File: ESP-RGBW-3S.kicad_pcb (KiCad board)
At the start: 2 copper layers, 66.7 x 48.3 mm, 39 parts, among them J1 12V IN, J2 PROG, J3 LED Str., J4 Temp. S., J5 Light. S., J6 PIR, Q1 IRLML0040TRPBF, Q2 IRLML0040TRPBF, Q3 IRLML0040TRPBF, Q4 IRLML0040TRPBF, SW1 Flash, U2 ESP-12E, U4 DCDC_LM2596

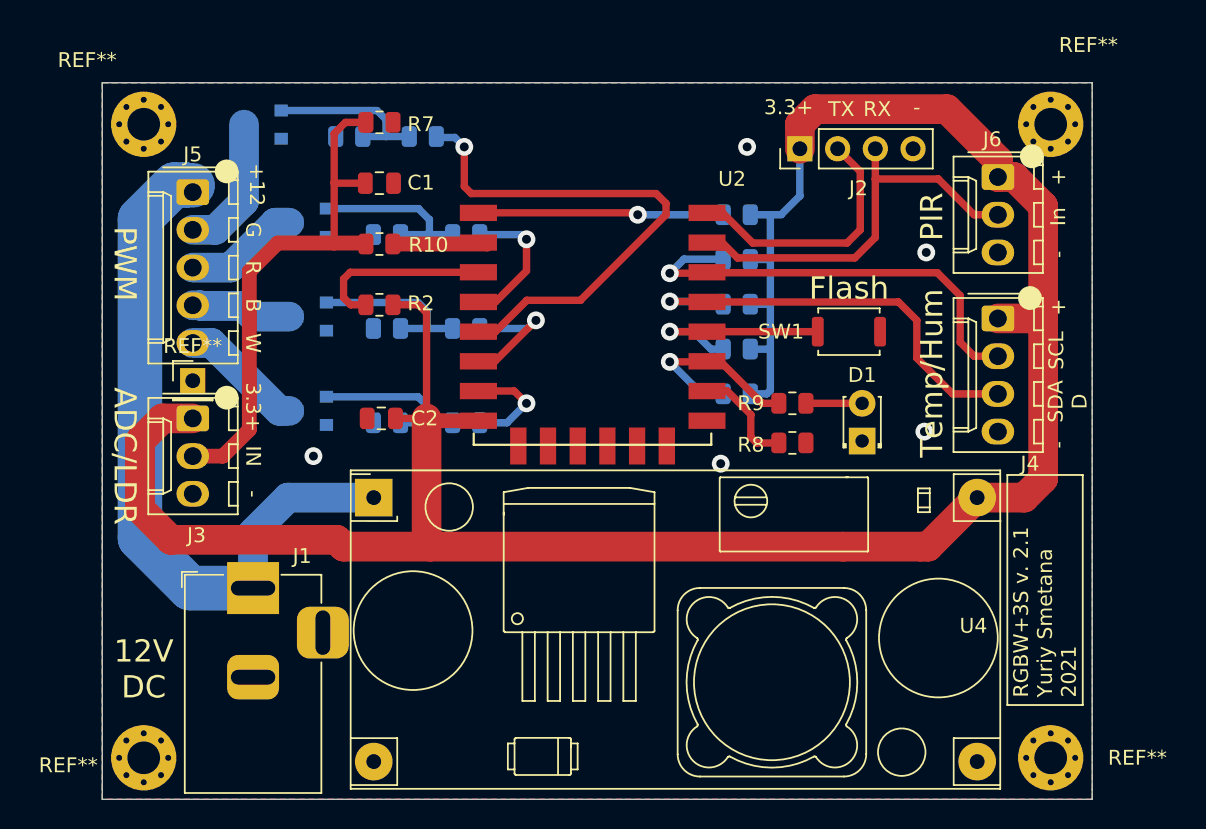
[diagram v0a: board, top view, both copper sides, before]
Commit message: silc correction, optional extra GND for J6
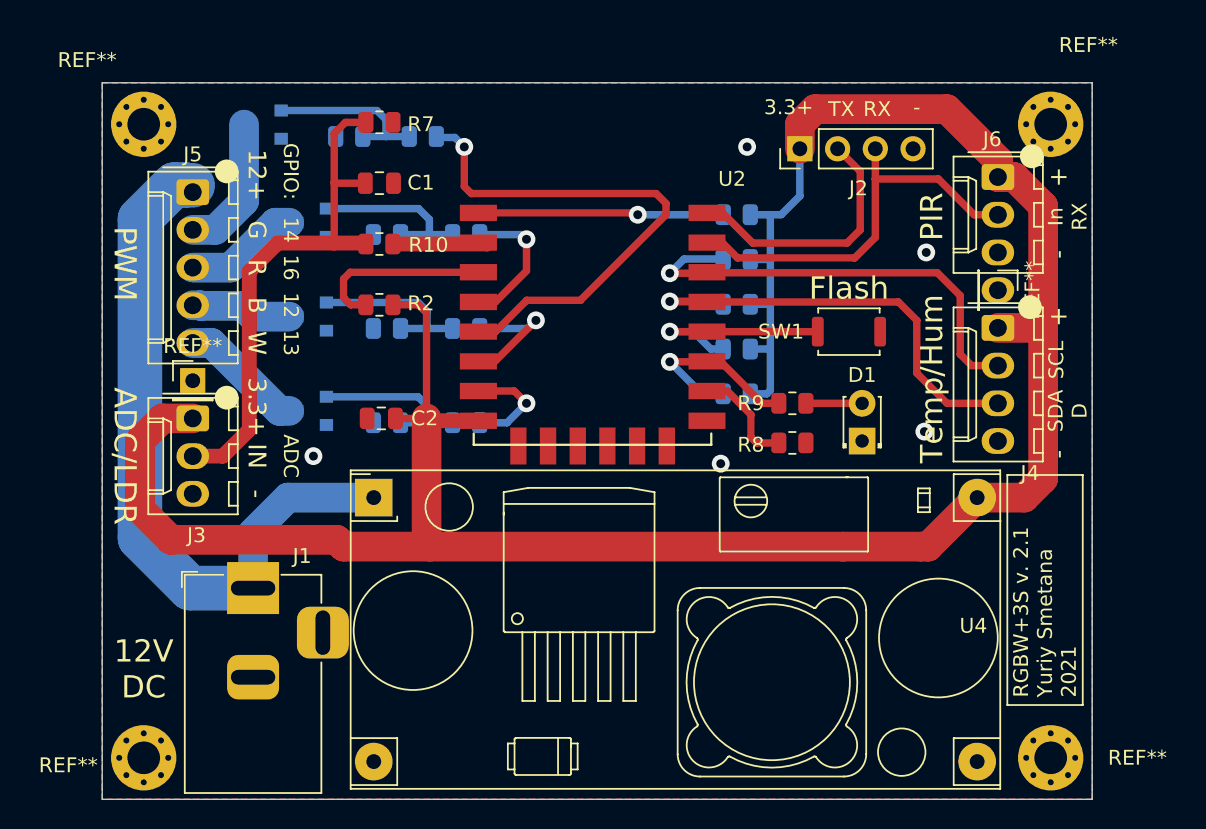
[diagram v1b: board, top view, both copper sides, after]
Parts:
- added REF**: PinHeader_1x01_P2.54mm_Vertical, Connector_PinHeader_2.54mm:PinHeader_1x01_P2.54mm_Vertical, F.Cu at (79.4, 39.4)
- moved J4 0.63 mm to (79.4, 41.9)
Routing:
- net /SDA-DATA: track 30.0 -> 30.8 mm
- net /SCL: track 30.9 -> 31.7 mm
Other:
- board text added: "12"
- board text added: "12+"
- board text added: "13"
- board text added: "14"
- board text added: "16"
- board text added: "ADC"
- board text added: "GPIO:"
- board text added: "In RX"
- board text removed: "+12"
- board text removed: "In"

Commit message: Update ESP-RGBW-3S.kicad_pcb
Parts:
- turned REF** to 270 degrees
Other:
- board text added: "RGBW-3S v. 2.3 Yuriy Smetana 2021"
- board text added: "RX In"
- board text removed: "In RX"
- board text removed: "RGBW+3S v. 2.1 Yuriy Smetana 2021"
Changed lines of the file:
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@@
   (page A4)
   (layers
-    (0 F.Cu signal)
+    (0 F.Cu signal hide)
     (31 B.Cu signal hide)
     (32 B.Adhes user hide)
@@
     (descr "Through hole straight pin header, 1x01, 2.54mm pitch, single row")
     (tags "Through hole pin header THT 1x01 2.54mm single row")
-    (fp_text reference REF** (at 0 -2.33 90) (layer F.SilkS)
+    (fp_text reference REF** (at -0.127 -7.747 90) (layer F.SilkS) hide
       (effects (font (size 1 1) (thickness 0.15)))
     )
@@
       (effects (font (size 1 1) (thickness 0.15)))
     )
-    (pad 6* thru_hole oval (at 0 0 270) (size 1.74 2.2) (drill 1.2) (layers *.Cu *.Mask)
+    (pad 4* thru_hole oval (at 0 0 270) (size 1.74 2.2) (drill 1.2) (layers *.Cu *.Mask)
       (net 1 GND))
     (model ${KISYS3DMOD}/Connector_PinHeader_2.54mm.3dshapes/PinHeader_1x01_P2.54mm_Vertical.wrl
@@
   )
   (module Connector_PinHeader_2.54mm:PinHeader_1x01_P2.54mm_Vertical (layer F.Cu)
-    (at 25.146 45.466)
+    (at 25.146 45.466 270)
     (descr "Through hole straight pin header, 1x01, 2.54mm pitch, single row")
     (tags "Through hole pin header THT 1x01 2.54mm single row")
-    (fp_text reference REF** (at 0 -2.33) (layer F.SilkS)
-      (effects (font (size 1 1) (thickness 0.15)))
-    )
-    (fp_text value PinHeader_1x01_P2.54mm_Vertical (at 0 2.33) (layer F.Fab)
-      (effects (font (size 1 1) (thickness 0.15)))
-    )
-    (fp_text user %R (at 0 0 90) (layer F.Fab)
+    (fp_text reference REF** (at 0 7.747 90) (layer F.SilkS) hide
+      (effects (font (size 1 1) (thickness 0.15)))
+    )
+    (fp_text value PinHeader_1x01_P2.54mm_Vertical (at 0 2.33 90) (layer F.Fab)
+      (effects (font (size 1 1) (thickness 0.15)))
+    )
+    (fp_text user %R (at 0 0) (layer F.Fab)
       (effects (font (size 1 1) (thickness 0.15)))
     )
@@
     (fp_line (start 1.8 1.8) (end 1.8 -1.8) (layer F.CrtYd) (width 0.05))
     (fp_line (start 1.8 -1.8) (end -1.8 -1.8) (layer F.CrtYd) (width 0.05))
-    (pad 6* thru_hole rect (at 0 0) (size 1.7 1.7) (drill 1) (layers *.Cu *.Mask)
+    (pad 6* thru_hole oval (at 0 0 270) (size 1.74 2.2) (drill 1.2) (layers *.Cu *.Mask)
       (net 1 GND))
     (model ${KISYS3DMOD}/Connector_PinHeader_2.54mm.3dshapes/PinHeader_1x01_P2.54mm_Vertical.wrl
@@
     (descr "Molex KK-254 Interconnect System, old/engineering part number: AE-6410-04A example for new part number: 22-27-2041, 4 Pins (http://www.molex.com/pdm_docs/sd/022272021_sd.pdf), generated with kicad-footprint-generator")
     (tags "connector Molex KK-254 side entry")
-    (fp_text reference J4 (at 9.779 -2.159 180) (layer F.SilkS)
+    (fp_text reference J4 (at 10.16 -2.413 180) (layer F.SilkS)
       (effects (font (size 1 1) (thickness 0.15)))
     )
@@
   (gr_line (start 19.05 73.025) (end 19.05 73.66) (layer Edge.Cuts) (width 0.05))
   (gr_line (start 85.725 73.025) (end 85.725 73.66) (layer Edge.Cuts) (width 0.05))
-  (gr_line (start 85.09 51.816) (end 80.01 51.816) (layer F.SilkS) (width 0.12))
-  (gr_line (start 85.09 67.31) (end 85.09 51.816) (layer F.SilkS) (width 0.12))
+  (gr_line (start 85.09 53.848) (end 80.01 53.848) (layer F.SilkS) (width 0.12))
+  (gr_line (start 85.09 67.31) (end 85.09 53.848) (layer F.SilkS) (width 0.12))
   (gr_line (start 80.01 67.31) (end 85.09 67.31) (layer F.SilkS) (width 0.12))
-  (gr_line (start 80.01 51.816) (end 80.01 67.31) (layer F.SilkS) (width 0.12))
+  (gr_line (start 80.01 53.848) (end 80.01 67.31) (layer F.SilkS) (width 0.12))
   (gr_text JLCJLCJLCJLC (at 29.972 70.866) (layer B.SilkS)
     (effects (font (size 1 1) (thickness 0.15)) (justify mirror))
   )
-  (gr_text "RGBW+3S v. 2.1\nYuriy Smetana\n2021" (at 82.55 66.802 90) (layer F.SilkS)
+  (gr_text "RGBW-3S v. 2.3\nYuriy Smetana\n2021" (at 82.55 66.802 90) (layer F.SilkS)
     (effects (font (size 1 1) (thickness 0.15)) (justify left))
   )
@@
     (effects (font (size 1.2 1.2) (thickness 0.2)))
   )
-  (gr_text "In\nRX" (at 84.074 34.417 90) (layer F.SilkS)
+  (gr_text "RX\nIn" (at 84.074 34.417 90) (layer F.SilkS)
     (effects (font (size 1 1) (thickness 0.2)))
   )
@@
   (segment (start 60.84125 37.27196) (end 60.87046 37.30117) (width 0.5) (layer B.Cu) (net 12))
   (segment (start 58.23204 37.27196) (end 60.84125 37.27196) (width 0.5) (layer B.Cu) (net 12))
-  (segment (start 75.296254 38.195022) (end 76.835 39.733768) (width 0.5) (layer F.Cu) (net 12))
-  (segment (start 59.117022 38.195022) (end 75.296254 38.195022) (width 0.5) (layer F.Cu) (net 12))
+  (segment (start 77.597 44.45) (end 79.375 44.45) (width 0.5) (layer F.Cu) (net 12))
+  (segment (start 76.835 40.513) (end 76.835 43.688) (width 0.5) (layer F.Cu) (net 12))
+  (segment (start 74.517022 38.195022) (end 76.835 40.513) (width 0.5) (layer F.Cu) (net 12))
+  (segment (start 59.117022 38.195022) (end 74.517022 38.195022) (width 0.5) (layer F.Cu) (net 12))
+  (segment (start 76.835 43.688) (end 77.597 44.45) (width 0.5) (layer F.Cu) (net 12))
   (segment (start 59.085 38.163) (end 59.117022 38.195022) (width 0.5) (layer F.Cu) (net 12))
-  (segment (start 76.835 39.733768) (end 76.835 43.688) (width 0.5) (layer F.Cu) (net 12))
-  (segment (start 77.597 44.45) (end 79.375 44.45) (width 0.5) (layer F.Cu) (net 12))
-  (segment (start 76.835 43.688) (end 77.597 44.45) (width 0.5) (layer F.Cu) (net 12))
   (via (at 57.277 40.132) (size 1.2) (drill 0.6) (layers F.Cu B.Cu) (net 13))
   (segment (start 57.15 40.132) (end 57.277 40.132) (width 0.5) (layer B.Cu) (net 13))

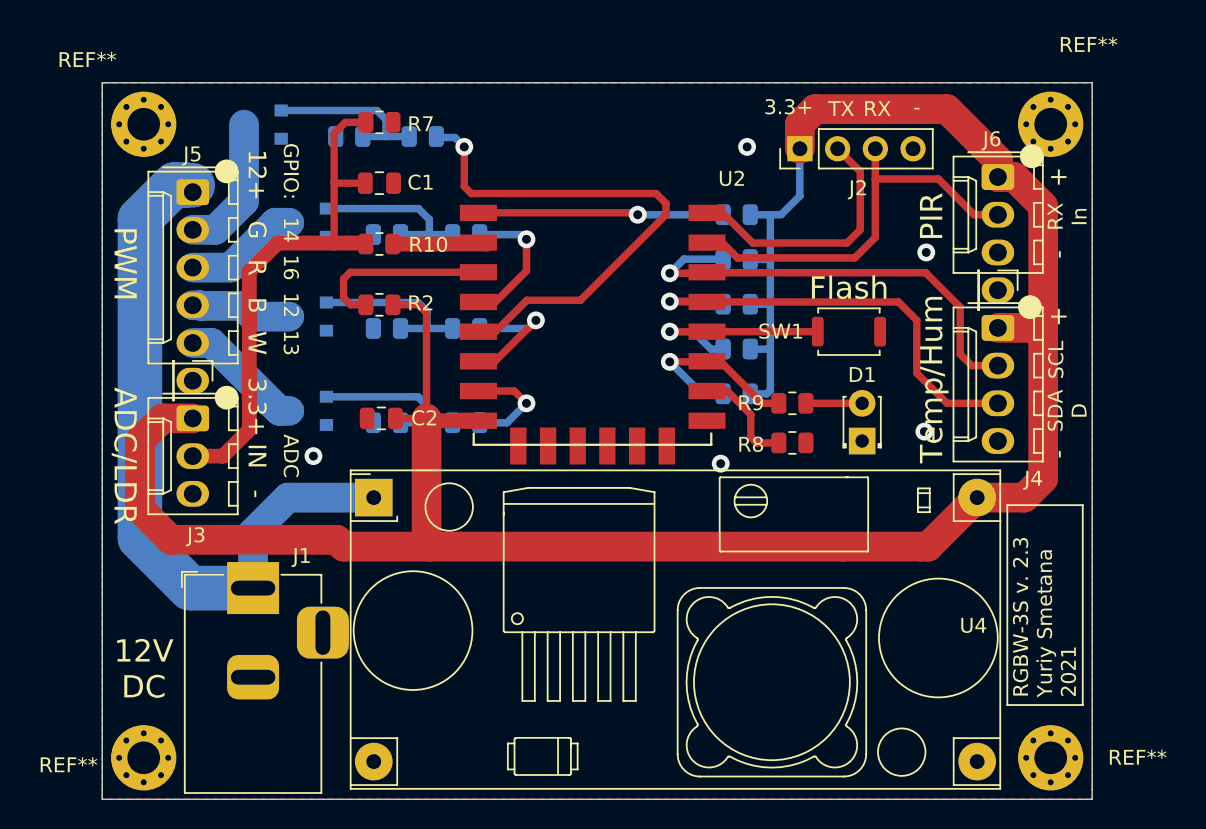
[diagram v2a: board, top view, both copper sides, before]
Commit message: v 0.4, pull-up option for GPIO 12-14
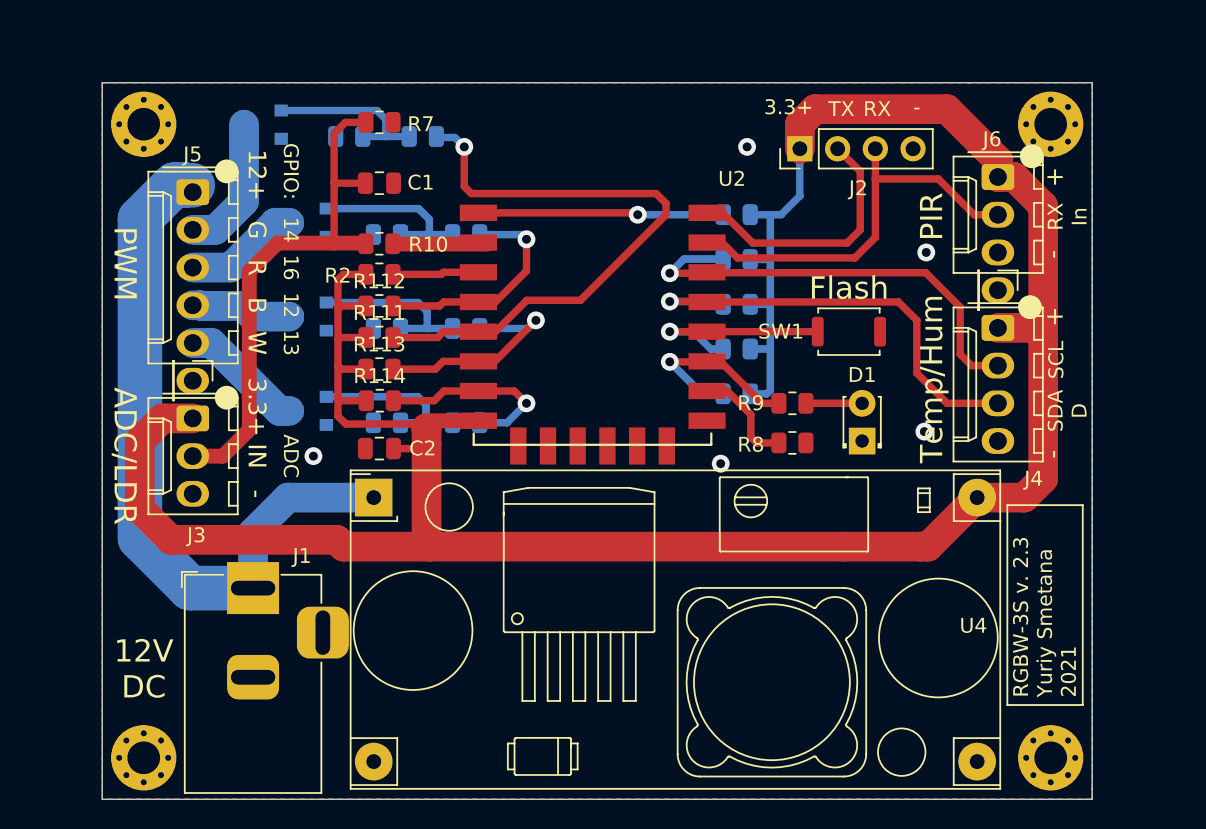
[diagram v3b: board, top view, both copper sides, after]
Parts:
- added R111: 10K, Resistor_SMD:R_0805_2012Metric, F.Cu at (37.7, 42.6)
- added R112: 10K, Resistor_SMD:R_0805_2012Metric, F.Cu at (37.7, 40.4)
- added R113: 10K, Resistor_SMD:R_0805_2012Metric, F.Cu at (37.7, 44.7)
- added R114: 10K, Resistor_SMD:R_0805_2012Metric, F.Cu at (37.7, 46.8)
- moved R2 2.05 mm to (37.7, 38.3), turned to 0 degrees
- moved C2 2.04 mm to (37.7, 50.0)
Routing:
- net +3V3: track 166.7 -> 181.8 mm
- net White: track 6.82 -> 13.5 mm
- net Blue: track 8.33 -> 15.0 mm
- net Green: track 35.0 -> 41.6 mm
- net Red: track 8.82 -> 15.4 mm
- net Net-(R2-Pad2): track 12.8 -> 6.51 mm

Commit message: pull-up resistors for GPIO 12-16 reposition
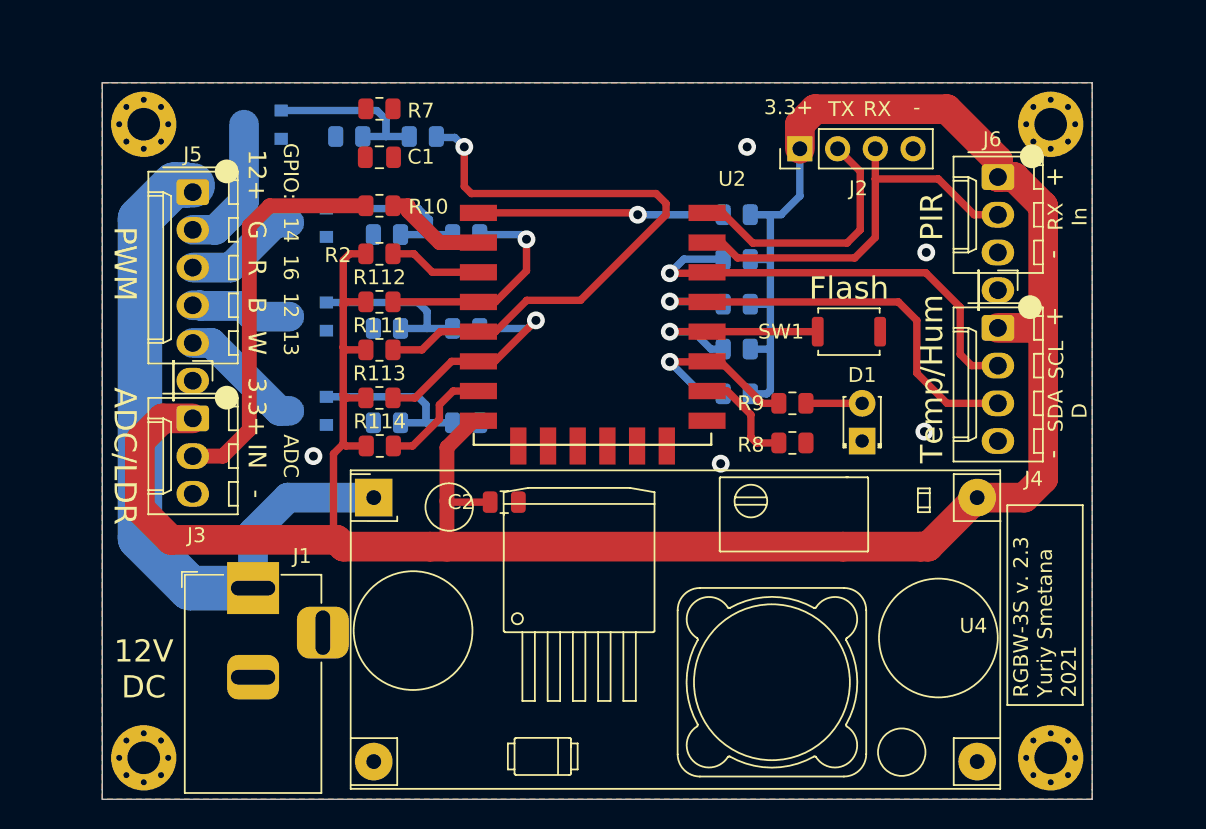
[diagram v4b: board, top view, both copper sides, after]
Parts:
- moved C2 9.15 mm to (46.1, 53.6), turned to 0 degrees
- moved R114 3.05 mm to (37.7, 49.9)
- moved R10 2.56 mm to (37.7, 33.7)
- moved R113 1.94 mm to (37.7, 46.6)
- moved C1 1.74 mm to (37.7, 30.4)
- moved R2 1.38 mm to (37.7, 36.9)
- moved R7 0.91 mm to (37.7, 27.2)
- moved R111 0.83 mm to (37.7, 43.4)
- moved R112 0.28 mm to (37.7, 40.2)
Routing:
- net ADC: track 35.3 -> 26.4 mm
- net White: track 13.5 -> 8.52 mm, vias 1 -> 0
- net +3V3: track 181.8 -> 184.8 mm
- net Net-(R10-Pad1): track 6.41 -> 7.69 mm
- net Blue: track 15.0 -> 16.1 mm

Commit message: optional pull-up and pull-down resistors for TX-RX
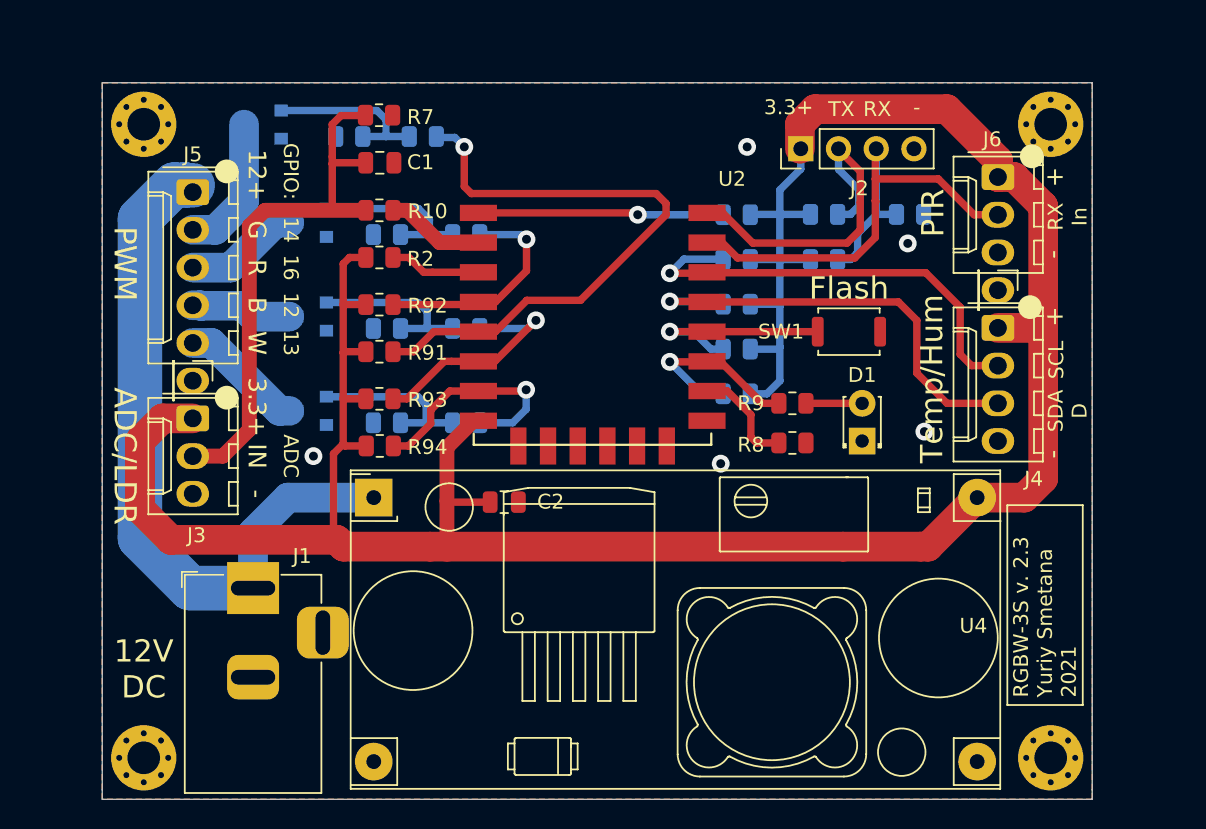
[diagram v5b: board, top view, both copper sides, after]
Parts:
- added R95: 10K, Resistor_SMD:R_0805_2012Metric, B.Cu at (67.7, 34.3)
- added R96: 10K, Resistor_SMD:R_0805_2012Metric, B.Cu at (67.7, 37.3)
- added R97: 10K, Resistor_SMD:R_0805_2012Metric, B.Cu at (73.5, 34.3)
- moved R7 0.43 mm to (37.7, 27.6)
- moved C1 0.37 mm to (37.7, 30.8)
- moved R10 0.31 mm to (37.7, 34.0)
- moved R2 0.25 mm to (37.7, 37.2)
- moved R92 0.19 mm to (37.7, 40.3)
- moved R91 0.12 mm to (37.7, 43.5)
- moved R93 0.06 mm to (37.7, 46.7)
- moved J2 0.06 mm to (66.1, 29.8)
- renumbered Q4 to Q1, Q3 to Q2, Q2 to Q3, Q1 to Q4, R18 to R12, R12 to R13, R17 to R14, R13 to R15, R14 to R17, R15 to R18, R111 to R91, R112 to R92, R113 to R93, R114 to R94
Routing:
- net ADC: track 26.4 -> 37.2 mm
- net RXD: track 28.3 -> 38.8 mm
- net White: track 8.52 -> 15.9 mm, vias 0 -> 1
- net TXD: track 18.3 -> 24.4 mm
- net +3V3: track 184.8 -> 190.7 mm
